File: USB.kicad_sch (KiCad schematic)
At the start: 19 parts, among them J501 USB_A, J502 USB_A, U501 ASDMB-24.000MHz-C, U502 ASDMB-26.000MHz-C, U503 USB3343, U504 74LVC1G07, U505 USB2514B_Bi

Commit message: Move Ethernet PHY to left side of board
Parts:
- C507: Rated Voltage (none) -> 10V; Voltage 10V -> (none)
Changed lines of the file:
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@@
-(kicad_sch (version 20200714) (host eeschema "5.99.0-unknown-829316fad~102~ubuntu20.04.1")
+(kicad_sch (version 20200828) (generator eeschema)
   (page 5 15)
   (paper "B")
@@
   (junction (at 212.09 116.84) (diameter 1.016) (color 0 0 0 0))
   (junction (at 252.73 148.59) (diameter 1.016) (color 0 0 0 0))
+  (no_connect (at 273.05 132.08))
+  (no_connect (at 273.05 119.38))
   (no_connect (at 179.07 134.62))
-  (no_connect (at 273.05 119.38))
-  (no_connect (at 273.05 132.08))
   (bus_entry (at 134.62 116.84) (size 2.54 2.54)
     (stroke (width 0.1524) (type solid) (color 0 0 0 0))
@@
     (stroke (width 0) (type solid) (color 0 0 0 0))
   )
-  (bus (pts (xy 134.62 115.57) (xy 134.62 119.38))
+  (bus (pts (xy 134.62 115.57) (xy 134.62 116.84))
+    (stroke (width 0) (type solid) (color 0 0 0 0))
+  )
+  (bus (pts (xy 134.62 116.84) (xy 134.62 119.38))
     (stroke (width 0) (type solid) (color 0 0 0 0))
   )
@@
     (stroke (width 0) (type solid) (color 0 0 0 0))
   )
-  (bus (pts (xy 134.62 121.92) (xy 134.62 127))
-    (stroke (width 0) (type solid) (color 0 0 0 0))
-  )
-  (bus (pts (xy 134.62 127) (xy 134.62 132.08))
-    (stroke (width 0) (type solid) (color 0 0 0 0))
-  )
-  (bus (pts (xy 134.62 132.08) (xy 134.62 137.16))
-    (stroke (width 0) (type solid) (color 0 0 0 0))
-  )
-  (bus (pts (xy 134.62 137.16) (xy 134.62 142.24))
+  (bus (pts (xy 134.62 121.92) (xy 134.62 124.46))
+    (stroke (width 0) (type solid) (color 0 0 0 0))
+  )
+  (bus (pts (xy 134.62 124.46) (xy 134.62 127))
+    (stroke (width 0) (type solid) (color 0 0 0 0))
+  )
+  (bus (pts (xy 134.62 127) (xy 134.62 129.54))
+    (stroke (width 0) (type solid) (color 0 0 0 0))
+  )
+  (bus (pts (xy 134.62 129.54) (xy 134.62 132.08))
+    (stroke (width 0) (type solid) (color 0 0 0 0))
+  )
+  (bus (pts (xy 134.62 132.08) (xy 134.62 134.62))
+    (stroke (width 0) (type solid) (color 0 0 0 0))
+  )
+  (bus (pts (xy 134.62 134.62) (xy 134.62 137.16))
+    (stroke (width 0) (type solid) (color 0 0 0 0))
+  )
+  (bus (pts (xy 134.62 137.16) (xy 134.62 139.7))
+    (stroke (width 0) (type solid) (color 0 0 0 0))
+  )
+  (bus (pts (xy 134.62 139.7) (xy 134.62 142.24))
     (stroke (width 0) (type solid) (color 0 0 0 0))
   )
@@
     (stroke (width 0) (type solid) (color 0 0 0 0))
   )
-  (bus (pts (xy 264.16 149.86) (xy 264.16 154.94))
+  (bus (pts (xy 264.16 149.86) (xy 264.16 152.4))
+    (stroke (width 0) (type solid) (color 0 0 0 0))
+  )
+  (bus (pts (xy 264.16 152.4) (xy 264.16 154.94))
     (stroke (width 0) (type solid) (color 0 0 0 0))
   )
@@
       (effects (font (size 1.27 1.27)) hide)
     )
-    (property "Voltage" "10V" (id 4) (at 208.6611 130.5687 0)
-      (effects (font (size 1.27 1.27)) (justify left))
-    )
-  )
+    (property "Rated Voltage" "10V" (id 4) (at 205.74 128.27 0)
+      (effects (font (size 1.27 1.27)) hide)
+    )
+  )

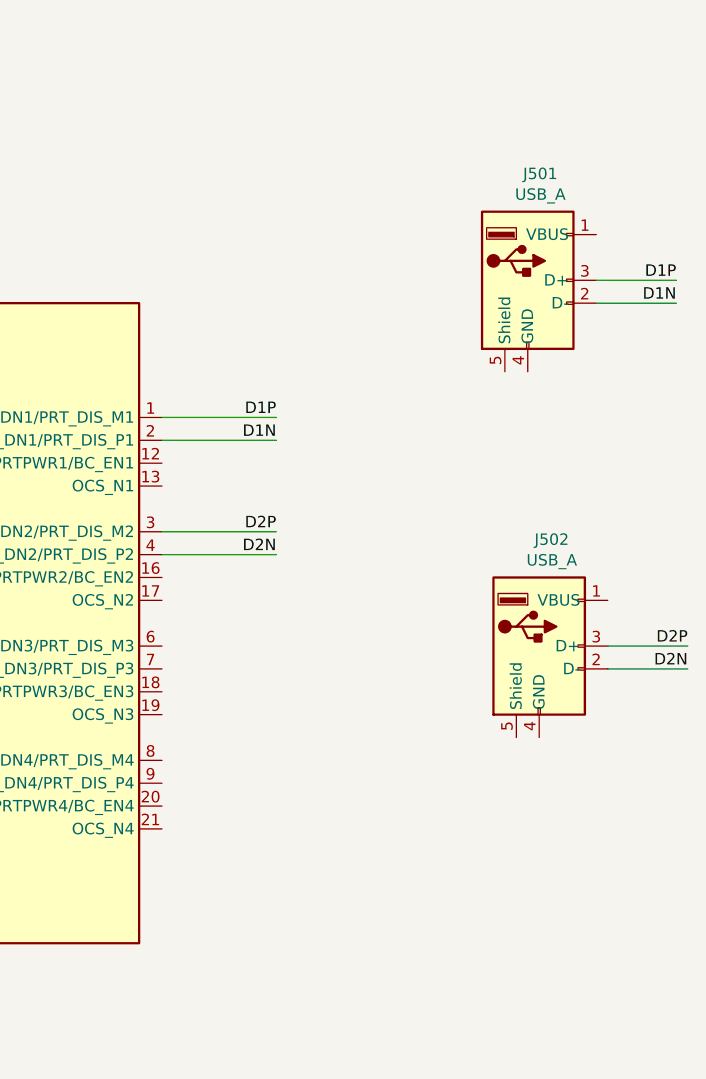
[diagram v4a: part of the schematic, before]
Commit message: Switch to stacked USB ports
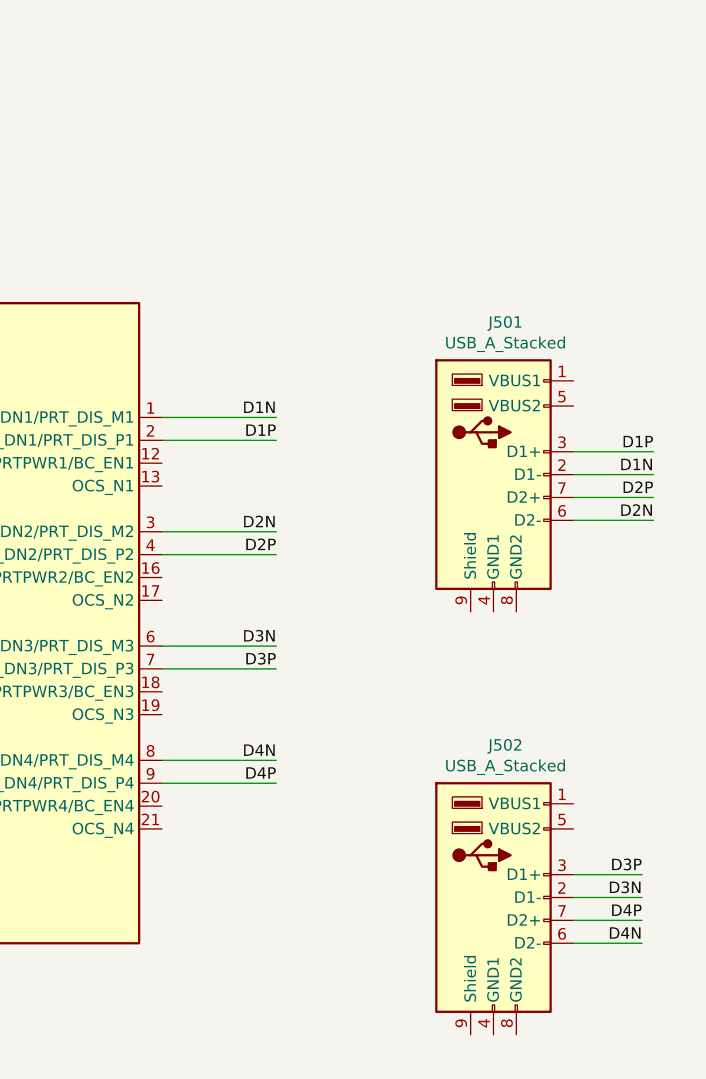
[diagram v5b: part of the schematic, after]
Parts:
- removed J501, J502: USB_A, Connector_USB:USB_A_Molex_67643_Horizontal, symbol Connector:USB_A
- added J501, J502: USB_A_Stacked, Connector_USB:USB_A_Wuerth_61400826021_Horizontal_Stacked, symbol Connector:USB_A_Stacked
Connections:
- net D1N: now also U505.1 (USBDM_DN1/PRT_DIS_M1), J501.2 (D1-); no longer U505.2 (USBDP_DN1/PRT_DIS_P1)
- net D1P: now also U505.2 (USBDP_DN1/PRT_DIS_P1), J501.3 (D1+); no longer U505.1 (USBDM_DN1/PRT_DIS_M1)
- net D2N: now also U505.3 (USBDM_DN2/PRT_DIS_M2), J501.6 (D2-); no longer U505.4 (USBDP_DN2/PRT_DIS_P2)
- net D2P: now also U505.4 (USBDP_DN2/PRT_DIS_P2), J501.7 (D2+); no longer U505.3 (USBDM_DN2/PRT_DIS_M2)
- net D3N: now reaches U505.6 (USBDM_DN3/PRT_DIS_M3)
- net D3N: now also J502.2 (D1-)
- net D3P: now reaches U505.7 (USBDP_DN3/PRT_DIS_P3)
- net D3P: now also J502.3 (D1+)
- net D4N: now reaches U505.8 (USBDM_DN4/PRT_DIS_M4)
- net D4N: now also J502.6 (D2-)
- net D4P: now reaches U505.9 (USBDP_DN4/PRT_DIS_P4)
- net D4P: now also J502.7 (D2+)
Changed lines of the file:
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@@
   (junction (at 212.09 116.84) (diameter 1.016) (color 0 0 0 0))
   (junction (at 252.73 148.59) (diameter 1.016) (color 0 0 0 0))
-  (no_connect (at 273.05 119.38))
   (no_connect (at 179.07 134.62))
   (no_connect (at 273.05 132.08))
+  (no_connect (at 273.05 119.38))
   (bus_entry (at 134.62 116.84) (size 2.54 2.54)
     (stroke (width 0.1524) (type solid) (color 0 0 0 0))
@@
     (stroke (width 0) (type solid) (color 0 0 0 0))
   )
-  (wire (pts (xy 377.19 88.9) (xy 386.08 88.9))
-    (stroke (width 0) (type solid) (color 0 0 0 0))
-  )
-  (wire (pts (xy 377.19 91.44) (xy 386.08 91.44))
-    (stroke (width 0) (type solid) (color 0 0 0 0))
-  )
-  (wire (pts (xy 378.46 129.54) (xy 387.35 129.54))
-    (stroke (width 0) (type solid) (color 0 0 0 0))
-  )
-  (wire (pts (xy 378.46 132.08) (xy 387.35 132.08))
+  (wire (pts (xy 328.93 129.54) (xy 341.63 129.54))
+    (stroke (width 0) (type solid) (color 0 0 0 0))
+  )
+  (wire (pts (xy 328.93 132.08) (xy 341.63 132.08))
+    (stroke (width 0) (type solid) (color 0 0 0 0))
+  )
+  (wire (pts (xy 328.93 142.24) (xy 341.63 142.24))
+    (stroke (width 0) (type solid) (color 0 0 0 0))
+  )
+  (wire (pts (xy 328.93 144.78) (xy 341.63 144.78))
+    (stroke (width 0) (type solid) (color 0 0 0 0))
+  )
+  (wire (pts (xy 374.65 107.95) (xy 383.54 107.95))
+    (stroke (width 0) (type solid) (color 0 0 0 0))
+  )
+  (wire (pts (xy 374.65 110.49) (xy 383.54 110.49))
+    (stroke (width 0) (type solid) (color 0 0 0 0))
+  )
+  (wire (pts (xy 374.65 113.03) (xy 383.54 113.03))
+    (stroke (width 0) (type solid) (color 0 0 0 0))
+  )
+  (wire (pts (xy 374.65 115.57) (xy 383.54 115.57))
+    (stroke (width 0) (type solid) (color 0 0 0 0))
+  )
+  (wire (pts (xy 374.65 154.94) (xy 382.27 154.94))
+    (stroke (width 0) (type solid) (color 0 0 0 0))
+  )
+  (wire (pts (xy 374.65 157.48) (xy 382.27 157.48))
+    (stroke (width 0) (type solid) (color 0 0 0 0))
+  )
+  (wire (pts (xy 374.65 160.02) (xy 382.27 160.02))
+    (stroke (width 0) (type solid) (color 0 0 0 0))
+  )
+  (wire (pts (xy 374.65 162.56) (xy 382.27 162.56))
     (stroke (width 0) (type solid) (color 0 0 0 0))
   )
@@
     (effects (font (size 1.27 1.27)) (justify right bottom))
   )
-  (label "D1P" (at 341.63 104.14 180)
-    (effects (font (size 1.27 1.27)) (justify right bottom))
-  )
-  (label "D1N" (at 341.63 106.68 180)
-    (effects (font (size 1.27 1.27)) (justify right bottom))
-  )
-  (label "D2P" (at 341.63 116.84 180)
-    (effects (font (size 1.27 1.27)) (justify right bottom))
-  )
-  (label "D2N" (at 341.63 119.38 180)
-    (effects (font (size 1.27 1.27)) (justify right bottom))
-  )
-  (label "D1P" (at 386.08 88.9 180)
-    (effects (font (size 1.27 1.27)) (justify right bottom))
-  )
-  (label "D1N" (at 386.08 91.44 180)
-    (effects (font (size 1.27 1.27)) (justify right bottom))
-  )
-  (label "D2P" (at 387.35 129.54 180)
-    (effects (font (size 1.27 1.27)) (justify right bottom))
-  )
-  (label "D2N" (at 387.35 132.08 180)
+  (label "D1N" (at 341.63 104.14 180)
+    (effects (font (size 1.27 1.27)) (justify right bottom))
+  )
+  (label "D1P" (at 341.63 106.68 180)
+    (effects (font (size 1.27 1.27)) (justify right bottom))
+  )
+  (label "D2N" (at 341.63 116.84 180)
+    (effects (font (size 1.27 1.27)) (justify right bottom))
+  )
+  (label "D2P" (at 341.63 119.38 180)
+    (effects (font (size 1.27 1.27)) (justify right bottom))
+  )
+  (label "D3N" (at 341.63 129.54 180)
+    (effects (font (size 1.27 1.27)) (justify right bottom))
+  )
+  (label "D3P" (at 341.63 132.08 180)
+    (effects (font (size 1.27 1.27)) (justify right bottom))
+  )
+  (label "D4N" (at 341.63 142.24 180)
+    (effects (font (size 1.27 1.27)) (justify right bottom))
+  )
+  (label "D4P" (at 341.63 144.78 180)
+    (effects (font (size 1.27 1.27)) (justify right bottom))
+  )
+  (label "D3P" (at 382.27 154.94 180)
+    (effects (font (size 1.27 1.27)) (justify right bottom))
+  )
+  (label "D3N" (at 382.27 157.48 180)
+    (effects (font (size 1.27 1.27)) (justify right bottom))
+  )
+  (label "D4P" (at 382.27 160.02 180)
+    (effects (font (size 1.27 1.27)) (justify right bottom))
+  )
+  (label "D4N" (at 382.27 162.56 180)
+    (effects (font (size 1.27 1.27)) (justify right bottom))
+  )
+  (label "D1P" (at 383.54 107.95 180)
+    (effects (font (size 1.27 1.27)) (justify right bottom))
+  )
+  (label "D1N" (at 383.54 110.49 180)
+    (effects (font (size 1.27 1.27)) (justify right bottom))
+  )
+  (label "D2P" (at 383.54 113.03 180)
+    (effects (font (size 1.27 1.27)) (justify right bottom))
+  )
+  (label "D2N" (at 383.54 115.57 180)
     (effects (font (size 1.27 1.27)) (justify right bottom))
   )
@@
     )
   )
-  (symbol (lib_id "Connector:USB_A") (at 369.57 88.9 0) (unit 1)
-    (in_bom yes) (on_board yes)
-    (property "Reference" "J501" (id 0) (at 370.967 77.0698 0))
-    (property "Value" "USB_A" (id 1) (at 370.967 79.3685 0))
-    (property "Footprint" "Connector_USB:USB_A_Molex_67643_Horizontal" (id 2) (at 373.38 90.17 0)
-      (effects (font (size 1.27 1.27)) hide)
-    )
-    (property "Datasheet" " ~" (id 3) (at 373.38 90.17 0)
-      (effects (font (size 1.27 1.27)) hide)
-    )
-  )
-  (symbol (lib_id "Connector:USB_A") (at 370.84 129.54 0) (unit 1)
-    (in_bom yes) (on_board yes)
-    (property "Reference" "J502" (id 0) (at 372.237 117.7098 0))
-    (property "Value" "USB_A" (id 1) (at 372.237 120.0085 0))
-    (property "Footprint" "Connector_USB:USB_A_Molex_67643_Horizontal" (id 2) (at 374.65 130.81 0)
-      (effects (font (size 1.27 1.27)) hide)
-    )
-    (property "Datasheet" " ~" (id 3) (at 374.65 130.81 0)
-      (effects (font (size 1.27 1.27)) hide)
-    )
-  )
   (symbol (lib_id "Oscillator:ASDMB-xxxMHz") (at 58.42 83.82 0) (unit 1)
     (in_bom yes) (on_board yes)
@@
       (effects (font (size 1.27 1.27)) hide)
     )
+  )
+  (symbol (lib_name "Connector:USB_A_Stacked_1") (lib_id "Connector:USB_A_Stacked") (at 365.76 110.49 0) (unit 1)
+    (in_bom yes) (on_board yes)
+    (property "Reference" "J501" (id 0) (at 367.1062 93.5798 0))
+    (property "Value" "USB_A_Stacked" (id 1) (at 367.1062 95.8785 0))
+    (property "Footprint" "Connector_USB:USB_A_Wuerth_61400826021_Horizontal_Stacked" (id 2) (at 370.84 109.22 0)
+      (effects (font (size 1.27 1.27)) hide)
+    )
+    (property "Datasheet" " ~" (id 3) (at 370.84 109.22 0)
+      (effects (font (size 1.27 1.27)) hide)
+    )
+  )
+  (symbol (lib_id "Connector:USB_A_Stacked") (at 365.76 157.48 0) (unit 1)
+    (in_bom yes) (on_board yes)
+    (property "Reference" "J502" (id 0) (at 367.1062 140.5698 0))
+    (property "Value" "USB_A_Stacked" (id 1) (at 367.1062 142.8685 0))
+    (property "Footprint" "Connector_USB:USB_A_Wuerth_61400826021_Horizontal_Stacked" (id 2) (at 370.84 156.21 0)
+      (effects (font (size 1.27 1.27)) hide)
+    )
+    (property "Datasheet" " ~" (id 3) (at 370.84 156.21 0)
+      (effects (font (size 1.27 1.27)) hide)
+    )

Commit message: Route ULPI signals
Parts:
- R501: footprint Resistor_SMD:R_0603_1608Metric -> Resistor_SMD:R_0402_1005Metric_Pad0.72x0.64mm_HandSolder
- R502, R503: footprint Resistor_SMD:R_0603_1608Metric -> Resistor_SMD:R_0402_1005Metric
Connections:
- net +3V3: now also C505.1, U503.16 (VBAT)
- net VDD18: now reaches C503.1, C504.1, U503.23 (VDD18), U503.9 (VDDIO)
- net RBIAS: now reaches R501.1, U503.19 (RBIAS)
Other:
- moved on the sheet: R501
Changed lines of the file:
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@@
   (junction (at 143.51 99.06) (diameter 1.016) (color 0 0 0 0))
   (junction (at 156.21 99.06) (diameter 1.016) (color 0 0 0 0))
+  (junction (at 168.91 99.06) (diameter 1.016) (color 0 0 0 0))
   (junction (at 205.74 121.92) (diameter 1.016) (color 0 0 0 0))
   (junction (at 212.09 116.84) (diameter 1.016) (color 0 0 0 0))
   (junction (at 252.73 148.59) (diameter 1.016) (color 0 0 0 0))
+  (no_connect (at 179.07 134.62))
   (no_connect (at 273.05 132.08))
-  (no_connect (at 179.07 134.62))
   (no_connect (at 273.05 119.38))
   (bus_entry (at 134.62 116.84) (size 2.54 2.54)
@@
     (stroke (width 0) (type solid) (color 0 0 0 0))
   )
+  (wire (pts (xy 168.91 91.44) (xy 168.91 99.06))
+    (stroke (width 0) (type solid) (color 0 0 0 0))
+  )
   (wire (pts (xy 168.91 99.06) (xy 168.91 106.68))
     (stroke (width 0) (type solid) (color 0 0 0 0))
@@
     (stroke (width 0) (type solid) (color 0 0 0 0))
   )
-  (wire (pts (xy 184.15 147.32) (xy 179.07 147.32))
-    (stroke (width 0) (type solid) (color 0 0 0 0))
-  )
-  (wire (pts (xy 184.15 149.86) (xy 184.15 147.32))
-    (stroke (width 0) (type solid) (color 0 0 0 0))
-  )
-  (wire (pts (xy 184.15 157.48) (xy 184.15 158.75))
+  (wire (pts (xy 185.42 147.32) (xy 179.07 147.32))
+    (stroke (width 0) (type solid) (color 0 0 0 0))
+  )
+  (wire (pts (xy 185.42 147.32) (xy 185.42 149.86))
+    (stroke (width 0) (type solid) (color 0 0 0 0))
+  )
+  (wire (pts (xy 185.42 157.48) (xy 185.42 158.75))
     (stroke (width 0) (type solid) (color 0 0 0 0))
   )
@@
   )
   (text "Layout note: place RBIAS resistor\nas close to USB3343 as possible."
-    (at 187.96 161.29 0)
+    (at 189.23 161.29 0)
     (effects (font (size 1.27 1.27)) (justify left bottom))
   )
@@
   )
   (label "USB.NXT" (at 147.32 147.32 180)
+    (effects (font (size 1.27 1.27)) (justify right bottom))
+  )
+  (label "VDD18" (at 153.67 99.06 180)
+    (effects (font (size 1.27 1.27)) (justify right bottom))
+  )
+  (label "RBIAS" (at 185.42 147.32 180)
     (effects (font (size 1.27 1.27)) (justify right bottom))
   )
@@
     )
   )
+  (symbol (lib_id "power:+3V3") (at 168.91 91.44 0) (unit 1)
+    (in_bom yes) (on_board yes)
+    (property "Reference" "#PWR?" (id 0) (at 168.91 95.25 0)
+      (effects (font (size 1.27 1.27)) hide)
+    )
+    (property "Value" "+3V3" (id 1) (at 169.2783 87.1156 0))
+    (property "Footprint" "" (id 2) (at 168.91 91.44 0)
+      (effects (font (size 1.27 1.27)) hide)
+    )
+    (property "Datasheet" "" (id 3) (at 168.91 91.44 0)
+      (effects (font (size 1.27 1.27)) hide)
+    )
+  )
   (symbol (lib_id "power:+1V8") (at 238.76 113.03 0) (unit 1)
     (in_bom yes) (on_board yes)
@@
     )
   )
-  (symbol (lib_id "power:GND") (at 184.15 158.75 0) (unit 1)
-    (in_bom yes) (on_board yes)
-    (property "Reference" "#PWR?" (id 0) (at 184.15 165.1 0)
-      (effects (font (size 1.27 1.27)) hide)
-    )
-    (property "Value" "GND" (id 1) (at 184.2643 163.0744 0))
-    (property "Footprint" "" (id 2) (at 184.15 158.75 0)
-      (effects (font (size 1.27 1.27)) hide)
-    )
-    (property "Datasheet" "" (id 3) (at 184.15 158.75 0)
+  (symbol (lib_id "power:GND") (at 185.42 158.75 0) (unit 1)
+    (in_bom yes) (on_board yes)
+    (property "Reference" "#PWR?" (id 0) (at 185.42 165.1 0)
+      (effects (font (size 1.27 1.27)) hide)
+    )
+    (property "Value" "GND" (id 1) (at 185.5343 163.0744 0))
+    (property "Footprint" "" (id 2) (at 185.42 158.75 0)
+      (effects (font (size 1.27 1.27)) hide)
+    )
+    (property "Datasheet" "" (id 3) (at 185.42 158.75 0)
       (effects (font (size 1.27 1.27)) hide)
     )
@@
       (effects (font (size 1.27 1.27)) (justify left))
     )
-    (property "Footprint" "Resistor_SMD:R_0603_1608Metric" (id 2) (at 251.46 125.73 0)
+    (property "Footprint" "Resistor_SMD:R_0402_1005Metric" (id 2) (at 251.46 125.73 0)
       (effects (font (size 1.27 1.27)) hide)
     )
@@
     )
   )
-  (symbol (lib_id "Device:R_US") (at 184.15 153.67 0) (unit 1)
-    (in_bom yes) (on_board yes)
-    (property "Reference" "R501" (id 0) (at 185.8011 152.5206 0)
+  (symbol (lib_id "Device:R_US") (at 185.42 153.67 0) (unit 1)
+    (in_bom yes) (on_board yes)
+    (property "Reference" "R501" (id 0) (at 187.0711 152.5206 0)
       (effects (font (size 1.27 1.27)) (justify left))
     )
-    (property "Value" "8.06k 1%" (id 1) (at 185.8011 154.8193 0)
+    (property "Value" "8.06k 1%" (id 1) (at 187.0711 154.8193 0)
       (effects (font (size 1.27 1.27)) (justify left))
     )
-    (property "Footprint" "Resistor_SMD:R_0603_1608Metric" (id 2) (at 185.166 153.924 90)
-      (effects (font (size 1.27 1.27)) hide)
-    )
-    (property "Datasheet" "~" (id 3) (at 184.15 153.67 0)
+    (property "Footprint" "Resistor_SMD:R_0402_1005Metric_Pad0.72x0.64mm_HandSolder" (id 2) (at 186.436 153.924 90)
+      (effects (font (size 1.27 1.27)) hide)
+    )
+    (property "Datasheet" "~" (id 3) (at 185.42 153.67 0)
       (effects (font (size 1.27 1.27)) hide)
     )
@@
     (property "Reference" "R502" (id 0) (at 196.85 124.7204 90))
     (property "Value" "10k 1/16W" (id 1) (at 196.85 127.0191 90))
-    (property "Footprint" "Resistor_SMD:R_0603_1608Metric" (id 2) (at 197.104 120.904 90)
-      (effects (font (size 1.27 1.27)) hide)
-    )
+    (property "Footprint" "Resistor_SMD:R_0402_1005Metric" (id 2) (at 197.104 120.904 90)
+      (effects (font (size 1.27 1.27)) hide)
+    )
